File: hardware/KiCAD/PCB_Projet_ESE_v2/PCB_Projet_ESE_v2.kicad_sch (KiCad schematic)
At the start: 50 parts, among them J1 Conn_01x06, J16 Conn_01x04, J2 Conn_01x04, J3 Conn_01x06, J4 Conn_01x03, J7 Conn_01x04, J8 Conn_01x02, J9 Conn_ST_STDC14, SW1 SW_SPST, SW2 472121010111, U1 ZXBM5210-SP, U2 ZXBM5210-SP, U3 STM32G474RETx, U4 ADXL343

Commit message: Finished Pinout v2
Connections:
- net +3.3V: now also J9.3 (VCC)
- net GND: now also U4.12 (SDO/ADDR)
- no-connect marks 9 -> 6

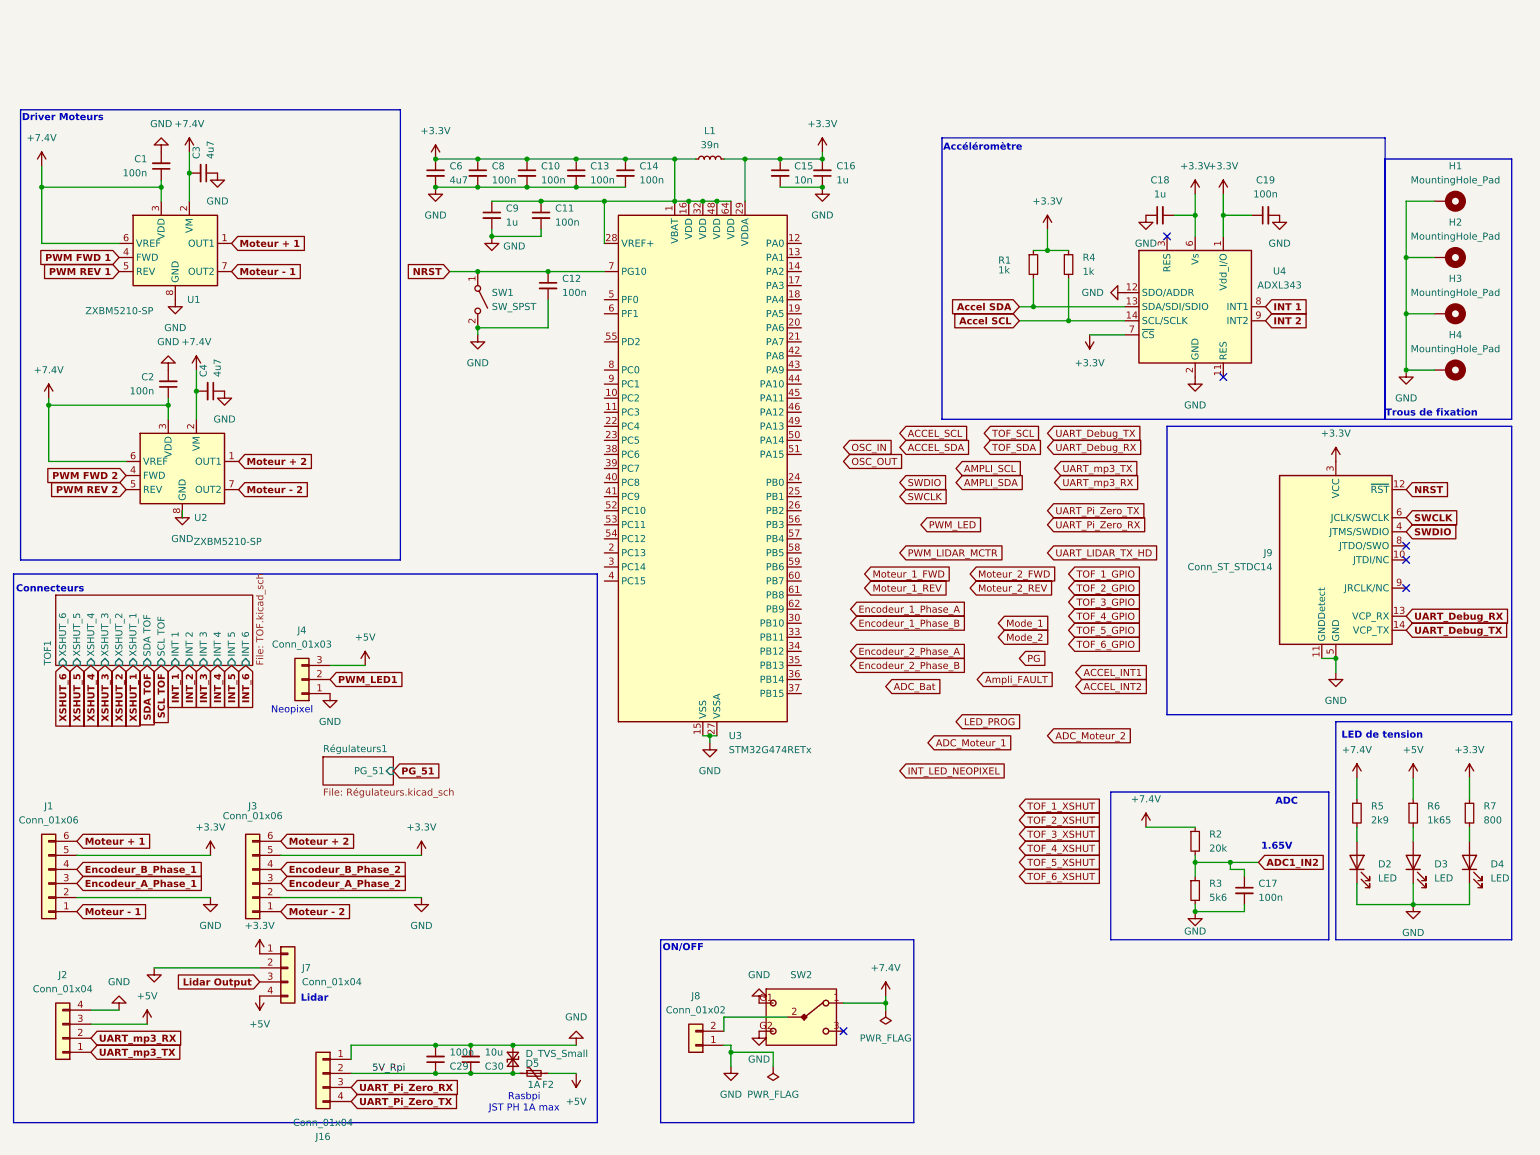
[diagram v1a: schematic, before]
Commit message: Schematic done for PCB v2
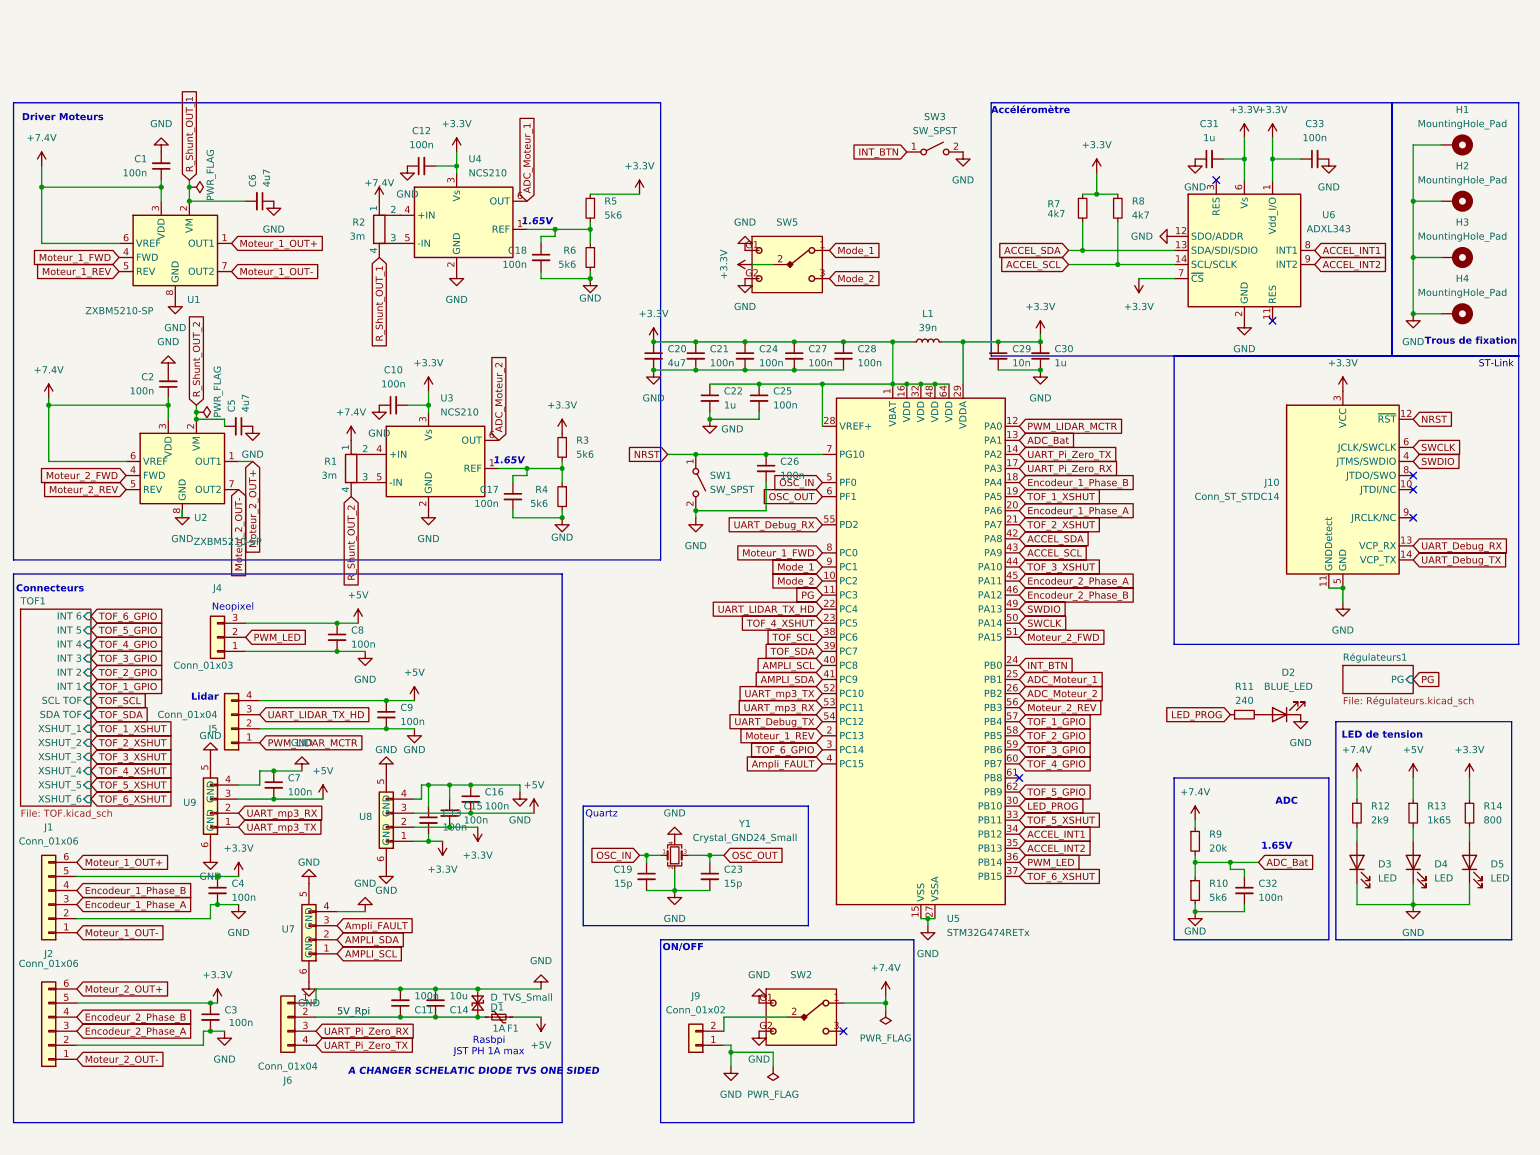
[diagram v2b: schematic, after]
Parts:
- removed J2: Conn_01x04, Connector_JST:JST_SH_BM04B-SRSS-TB_1x04-1MP_P1.00mm_Vertical, symbol Connector_Generic:Conn_01x04
- added C10, C12, C13, C15, C16, C17, C18, C3, C4, C7, C8, C9: 100n, Capacitor_SMD:C_0402_1005Metric, symbol Device:C_Small
- added C19, C23: 15p, Capacitor_SMD:C_0603_1608Metric, symbol Device:C_Small
- added D2: BLUE_LED, LED_SMD:LED_0603_1608Metric, symbol Device:LED
- added R1, R2: 3m, Resistor_SMD:R_Shunt_Vishay_WSK2512_6332Metric_T2.21mm, symbol Device:R_Shunt
- added R11: 240, Resistor_SMD:R_0402_1005Metric, symbol Device:R_Small
- added R3, R4, R5, R6: 5k6, Resistor_SMD:R_0402_1005Metric, symbol Device:R_Small
- added SW3: SW_SPST, mylib:SW_SPST, symbol Switch:SW_SPST
- added SW5: 472121010111, mylib:472123010111, symbol New_Library:472121010111
- added U3, U4: NCS210, Package_TO_SOT_SMD:SOT-363_SC-70-6, symbol Amplifier_Current:NCS210
- added U7, U8, U9: ~, mylib:JST_SH_4_Vertical, symbol my_lib:JST_SH_4_Vertical
- added Y1: Crystal_GND24_Small, Crystal:Crystal_SMD_3225-4Pin_3.2x2.5mm, symbol Device:Crystal_GND24_Small
- R7: renamed from R1; value 1k -> 4k7
- R8: renamed from R4; value 1k -> 4k7
- SW2: footprint mylib:SW_Wurth_WS-TOTV_472123020421 -> mylib:472123010111
- renumbered C29 to C11, C30 to C14, C6 to C20, C8 to C21, C9 to C22, C10 to C24, C11 to C25, C12 to C26, C13 to C27, C14 to C28, C15 to C29, C16 to C30, C18 to C31, C17 to C32, C19 to C33, C4 to C5, C3 to C6, D5 to D1, D2 to D3, D3 to D4, D4 to D5, F2 to F1, J9 to J10, J3 to J2, J7 to J5, J16 to J6, J8 to J9, R3 to R10, R5 to R12, R6 to R13, R7 to R14, R2 to R9, U3 to U5, U4 to U6
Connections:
- net ADC1_IN2 is gone; now on net ADC_Bat: C32.1, R10.1, R9.2
- net Accel SCL is gone; now on net ACCEL_SCL: R8.2, U6.14 (SCL/SCLK)
- net Accel SDA is gone; now on net ACCEL_SDA: R7.2, U6.13 (SDA/SDI/SDIO)
- net Encodeur_A_Phase_1 is gone; now on net Encodeur_1_Phase_A: J1.3 (Pin_3)
- net Encodeur_A_Phase_2 is gone; now on net Encodeur_2_Phase_A: J2.3 (Pin_3)
- net Encodeur_B_Phase_1 is gone; now on net Encodeur_1_Phase_B: J1.4 (Pin_4)
- net Encodeur_B_Phase_2 is gone; now on net Encodeur_2_Phase_B: J2.4 (Pin_4)
- net INT 1 is gone; now on net ACCEL_INT1: U6.8 (INT1)
- net INT 2 is gone; now on net ACCEL_INT2: U6.9 (INT2)
- net Lidar Output  is gone; now on net UART_LIDAR_TX_HD: J5.3 (Pin_3)
- net PWM FWD 1 is gone; now on net Moteur_1_FWD: U1.4 (FWD)
- net PWM FWD 2 is gone; now on net Moteur_2_FWD: U2.4 (FWD)
- net PWM REV 1 is gone; now on net Moteur_1_REV: U1.5 (REV)
- net PWM REV 2 is gone; now on net Moteur_2_REV: U2.5 (REV)
- net PWM_LED1 is gone; now on net PWM_LED: J4.2 (Pin_2)
- net +3.3V: now also C10.2, C12.2, C13.2, C15.2, C3.1, C4.1, R3.1, R5.1, SW5.2, U3.3 (Vs), U4.3 (Vs), U8.1, U8.2; no longer J5.1 (Pin_1)
- net +5V: now also C16.2, C7.2, C8.1, C9.1, U8.3, U9.3
- net +7.4V: now also R1.1, R2.1; no longer C5.2, C6.2, U1.2 (VM), U2.2 (VM)
- net ACCEL_INT1: now also U5.34 (PB12)
- net ACCEL_INT2: now also U5.35 (PB13)
- net ACCEL_SCL: now also U5.43 (PA9)
- net ACCEL_SDA: now also U5.42 (PA8)
- net ADC_Bat: now also U5.13 (PA1)
- net ADC_Moteur_1: now also U5.25 (PB1), U4.6 (OUT)
- net ADC_Moteur_2: now also U5.26 (PB2), U3.6 (OUT)
- net AMPLI_SCL: now also U5.40 (PC8), U7.1
- net AMPLI_SDA: now also U5.41 (PC9), U7.2
- net Ampli_FAULT: now also U5.4 (PC15), U7.3
- net Encodeur_1_Phase_A: now also U5.20 (PA6)
- net Encodeur_1_Phase_B: now also U5.18 (PA4)
- net Encodeur_2_Phase_A: now also U5.45 (PA11)
- net Encodeur_2_Phase_B: now also U5.46 (PA12)
- net GND: now also C10.1, C12.1, C13.1, C15.1, C16.1, C17.2, C18.2, C19.2, C23.2, C3.2, C4.2, C7.1, C8.2, C9.2, D2.1 (K), R4.2, R6.2, SW3.2 (B), SW5.G1, SW5.G2, U3.2 (GND), U4.2 (GND), U7.4, U7.5 (GND), U7.6 (GND), U8.4, U8.5 (GND), U8.6 (GND), U9.4, U9.5 (GND), U9.6 (GND), Y1.2, Y1.4
- net LED_PROG: now also U5.30 (PB10), R11.1
- net Mode_1: now also U5.9 (PC1), SW5.1
- net Mode_2: now also U5.10 (PC2), SW5.3
- net Moteur_1_FWD: now also U5.8 (PC0)
- net Moteur_1_REV: now also U5.2 (PC13)
- net Moteur_2_FWD: now also U5.51 (PA15)
- net Moteur_2_REV: now also U5.56 (PB3)
- net OSC_IN: now also U5.5 (PF0), C19.1, Y1.1
- net OSC_OUT: now also U5.6 (PF1), C23.1, Y1.3
- net PG: now also U5.11 (PC3)
- net PWM_LED: now also U5.36 (PB14)
- net PWM_LIDAR_MCTR: now also J5.1 (Pin_1), U5.12 (PA0)
- net SWCLK: now also U5.50 (PA14)
- net SWDIO: now also U5.49 (PA13)
- net TOF_1_GPIO: now also U5.57 (PB4)
- net TOF_1_XSHUT: now also U5.19 (PA5)
- net TOF_2_GPIO: now also U5.58 (PB5)
- net TOF_2_XSHUT: now also U5.21 (PA7)
- net TOF_3_GPIO: now also U5.59 (PB6)
- net TOF_3_XSHUT: now also U5.44 (PA10)
- net TOF_4_GPIO: now also U5.60 (PB7)
- net TOF_4_XSHUT: now also U5.23 (PC5)
- net TOF_5_GPIO: now also U5.62 (PB9)
- net TOF_5_XSHUT: now also U5.33 (PB11)
- net TOF_6_GPIO: now also U5.3 (PC14)
- net TOF_6_XSHUT: now also U5.37 (PB15)
- net TOF_SCL: now also U5.38 (PC6)
- net TOF_SDA: now also U5.39 (PC7)
- net UART_Debug_RX: now also U5.55 (PD2)
- net UART_Debug_TX: now also U5.54 (PC12)
- net UART_LIDAR_TX_HD: now also U5.22 (PC4)
- net UART_Pi_Zero_RX: now also U5.17 (PA3)
- net UART_Pi_Zero_TX: now also U5.14 (PA2)
- net UART_mp3_RX: now also U5.53 (PC11), U9.2
- net UART_mp3_TX: now also U5.52 (PC10), U9.1
- net INT_BTN: now reaches U5.24 (PB0)
- net INT_BTN: now also SW3.1 (A)
- net Moteur + 1 renamed Moteur_1_OUT+
- net Moteur + 2 renamed Moteur_2_OUT+
- net Moteur - 1 renamed Moteur_1_OUT-
- net Moteur - 2 renamed Moteur_2_OUT-
- new net: C17.1, R3.2, R4.1, U3.1 (REF)
- new net: C18.1, R5.2, R6.1, U4.1 (REF)
- new net: R1.2, U3.4 (+IN)
- new net: R1.3, U3.5 (-IN)
- new net: D2.2 (A), R11.2
- new net: R2.2, U4.4 (+IN)
- new net: R2.3, U4.5 (-IN)
- new net R_Shunt_OUT_1: C6.2, R2.4, U1.2 (VM)
- new net R_Shunt_OUT_2: C5.2, R1.4, U2.2 (VM)
- no-connect marks 6 -> 7
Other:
- sheet Régulateurs1 ports: added PG; removed PG_51
- note added: "A CHANGER SCHELATIC DIODE TVS ONE SIDED"
- note added: "Quartz"
- note added: "ST-Link"
- moved on the sheet: C11, C14, C20, C21, C22, C24, C25, C26, C27, C28, C29, C30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

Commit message: first version 52*52mm
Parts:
- removed SW2, SW5: 472121010111, mylib:472123010111, symbol New_Library:472121010111
- added C49: D8L6.5_865090349007, Capacitor_SMD_Wurth:CP_Wurth_WCAP-ASLU-D8L6.5, symbol Capacitor_Wurth_WCAP-ASLU:D8L6.5_865090349007
- added SW4, SW5: SW_SPDT, mylib:472123010111, symbol Switch:SW_SPDT
- H1: footprint MountingHole:MountingHole_3.2mm_M3_Pad_Via -> MountingHole:MountingHole_2.2mm_M2_Pad_Via
- H2, H3, H4: now left out of the parts list
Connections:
- net +3.3V: now also SW4.2 (B)
- net +5V: now also C49.1
- net +7.4V: now also SW5.1 (A)
- net GND: now also C49.2
- net Mode_1: now also SW4.1 (A)
- net Mode_2: now also SW4.3 (C)
- net at J9.2 (Pin_2): now also SW5.2 (B)

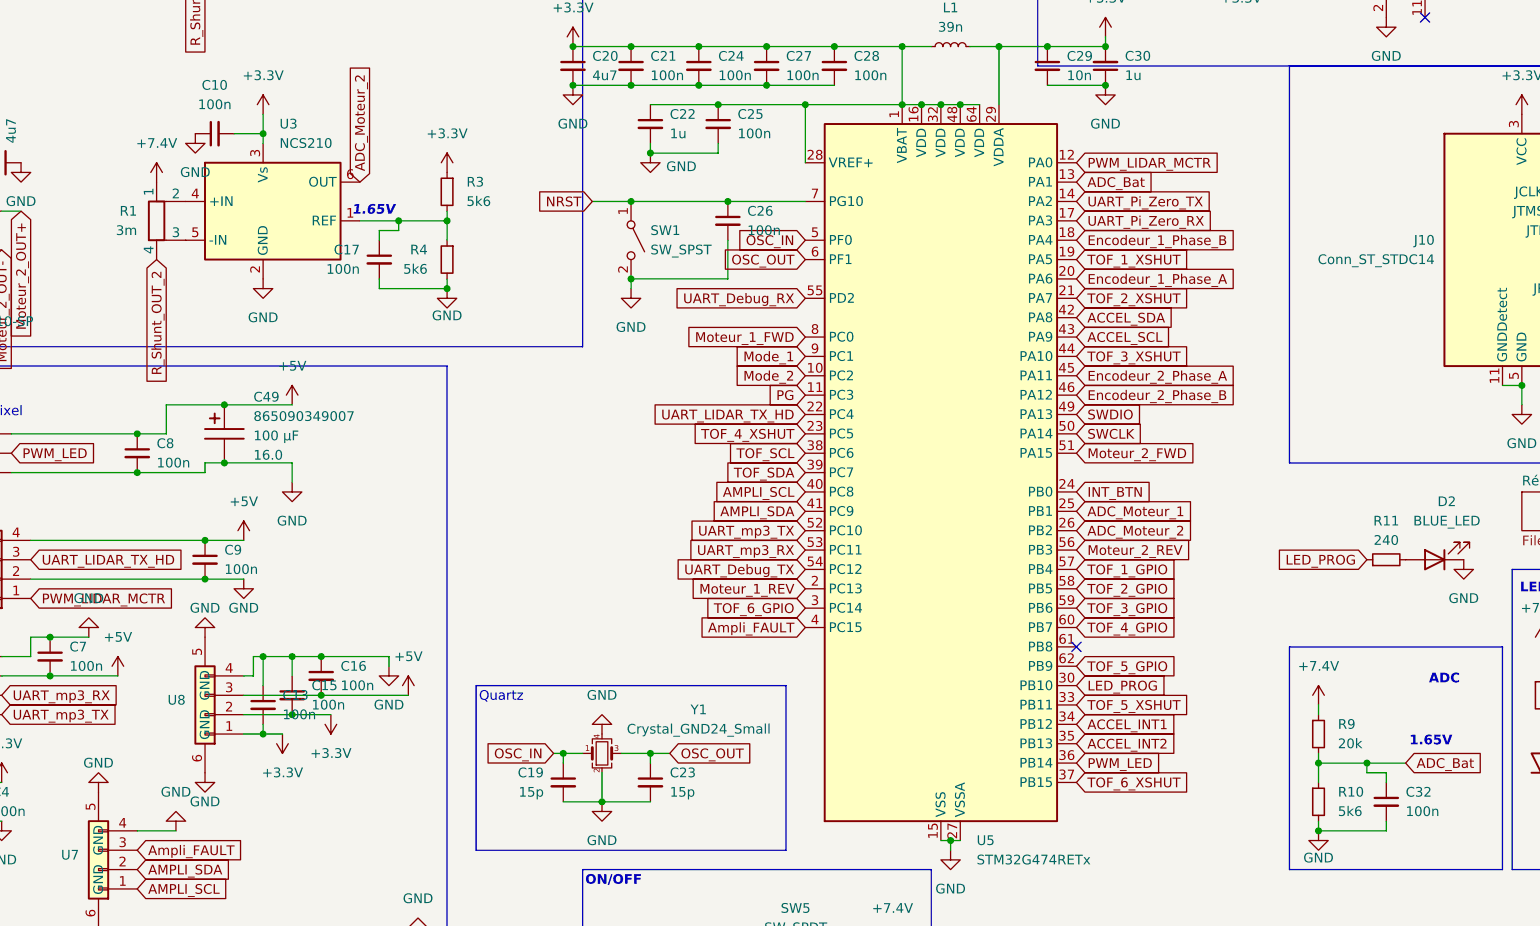
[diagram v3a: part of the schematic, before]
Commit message: new version 47x47mm
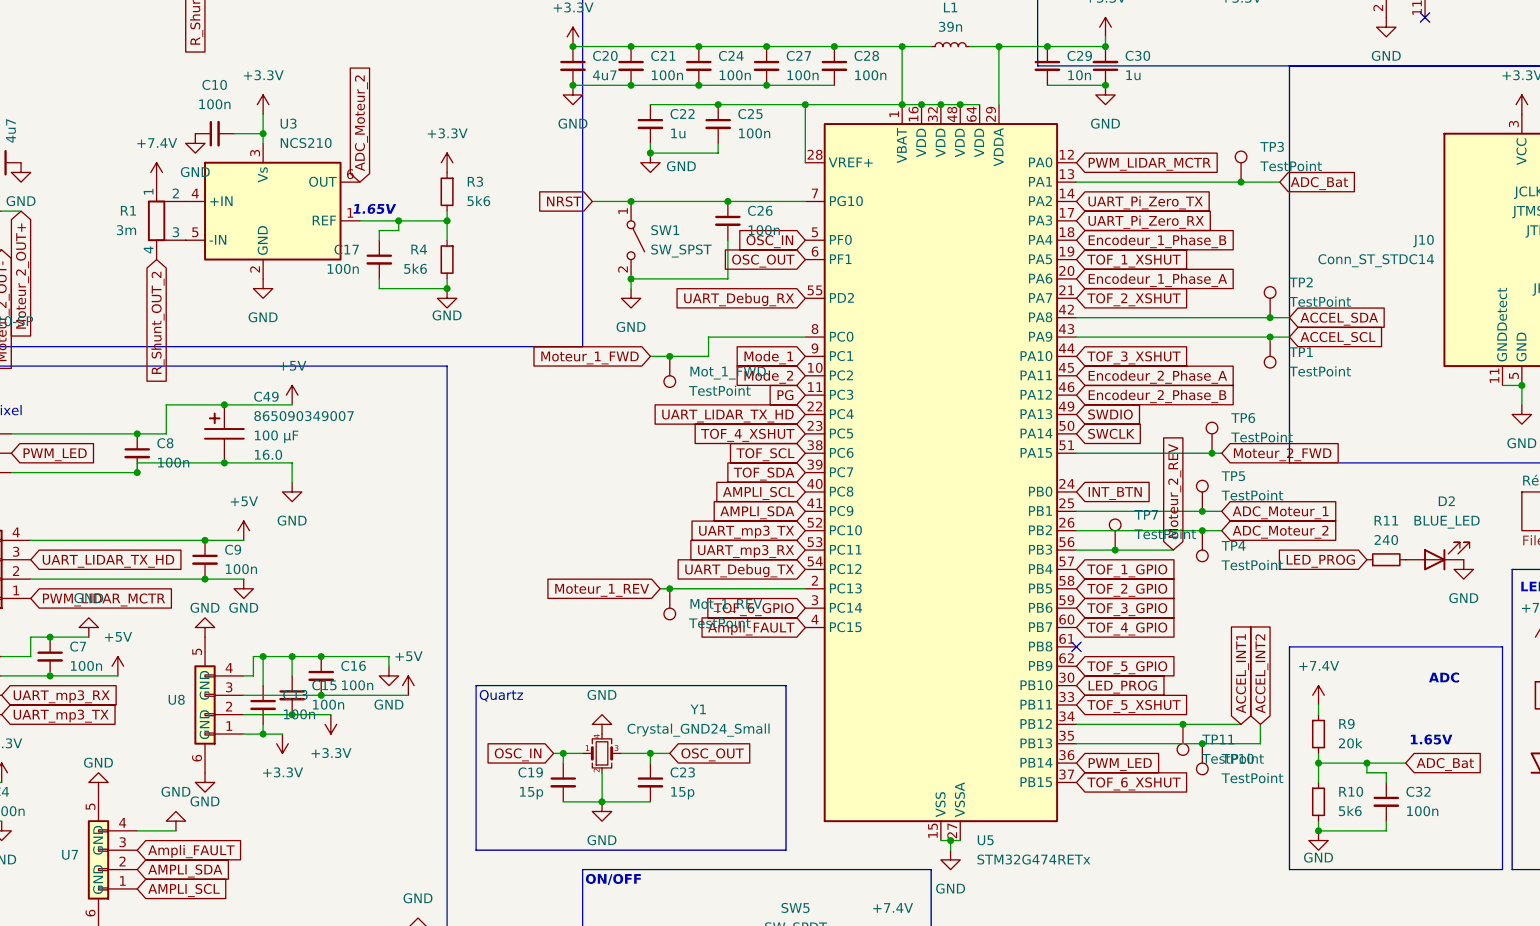
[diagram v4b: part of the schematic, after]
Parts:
- added Mot_1_FWD, Mot_1_REV, TP1, TP10, TP11, TP2, TP3, TP4, TP5, TP6, TP7: TestPoint, TestPoint:TestPoint_Pad_D2.0mm, symbol Connector:TestPoint
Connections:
- net ACCEL_INT1: now also TP11.1
- net ACCEL_INT2: now also TP10.1
- net ACCEL_SCL: now also TP1.1
- net ACCEL_SDA: now also TP2.1
- net ADC_Bat: now also TP3.1
- net ADC_Moteur_1: now also TP5.1
- net ADC_Moteur_2: now also TP4.1
- net Moteur_1_FWD: now also Mot_1_FWD.1
- net Moteur_1_REV: now also Mot_1_REV.1
- net Moteur_2_FWD: now also TP6.1
- net Moteur_2_REV: now also TP7.1
